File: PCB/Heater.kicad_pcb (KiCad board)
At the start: 2 copper layers, 29 parts, among them IC1 ATTINY45-P, P1 220V 50Hz, P2 ICP, P3 DS18B20, T1 SCR

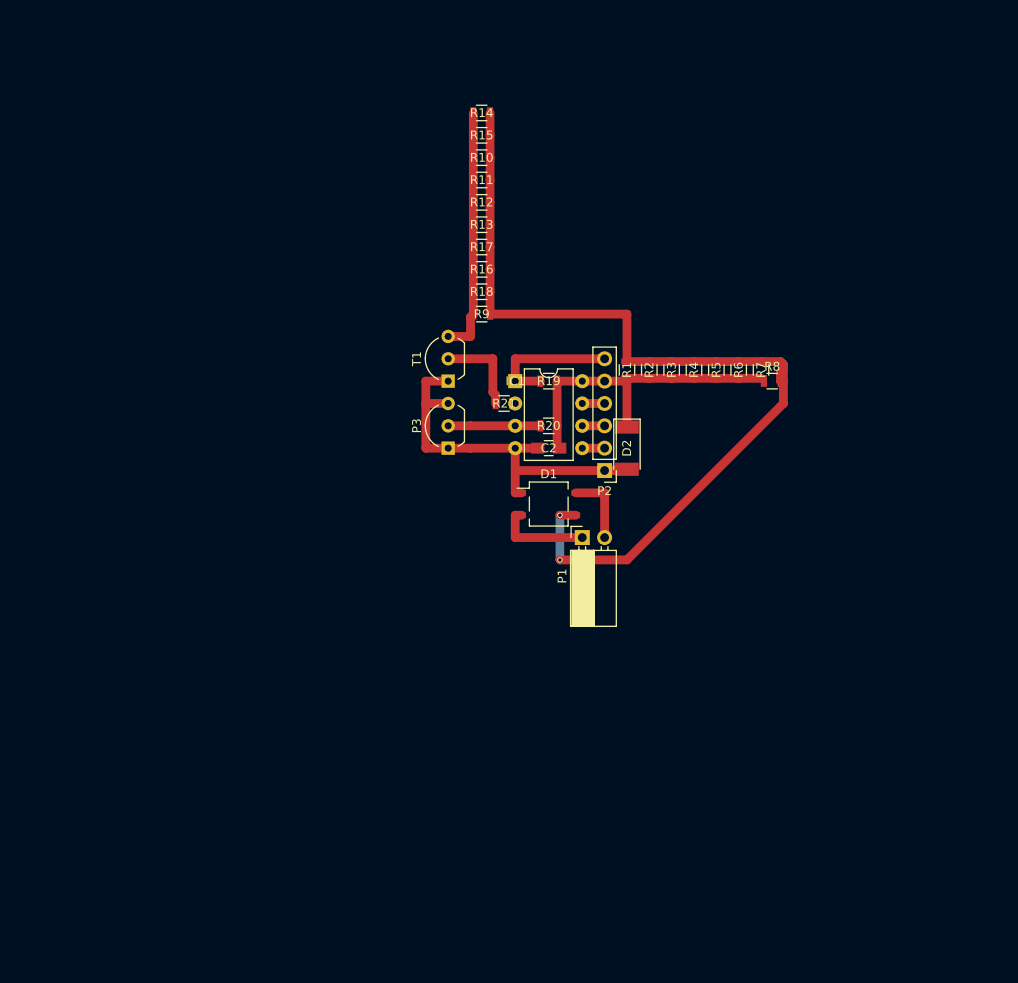
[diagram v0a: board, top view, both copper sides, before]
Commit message: Updated Schematic and PCB to use optotriac
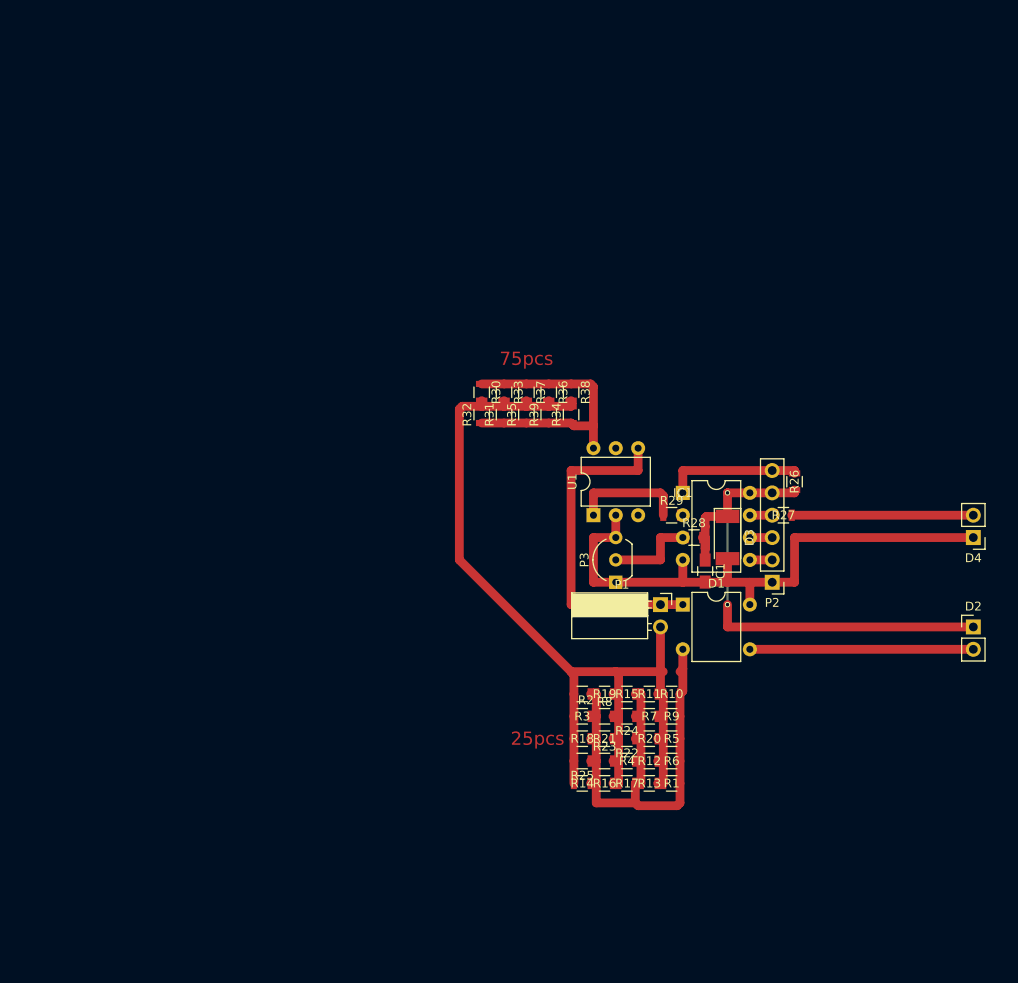
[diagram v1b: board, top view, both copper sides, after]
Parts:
- removed C2: 10u, Capacitors_SMD:C_0805_HandSoldering
- removed T1: SCR, TO_SOT_Packages_THT:TO-92_Inline_Wide
- added C1: 10u, Capacitors_SMD:C_0805_HandSoldering, F.Cu at (114.3, 94.0)
- added D3: ZD5V, Diodes_SMD:D_MELF, F.Cu at (116.8, 90.2)
- added D4: LED, Socket_Strips:Socket_Strip_Straight_1x02_Pitch2.54mm, F.Cu at (144.8, 90.2)
- added R22: 560K, Resistors_SMD:R_0805, F.Cu at (105.4, 113.0)
- added R23: 560K, Resistors_SMD:R_0805, F.Cu at (102.9, 115.6)
- added R24: 560K, Resistors_SMD:R_0805, F.Cu at (105.4, 110.5)
- added R25: 560K, Resistors_SMD:R_0805, F.Cu at (100.3, 115.6)
- added R26: 10K, Resistors_SMD:R_0805, F.Cu at (124.5, 83.8)
- added R27: 2K2, Resistors_SMD:R_0805, F.Cu at (123.2, 87.6)
- added R28: 5K, Resistors_SMD:R_0805, F.Cu at (113.0, 90.2)
- added R29: 470R, Resistors_SMD:R_0805, F.Cu at (110.5, 87.6)
- added R30: 560K, Resistors_SMD:R_0805, F.Cu at (88.9, 73.7)
- added R31: 560K, Resistors_SMD:R_0805, F.Cu at (91.4, 76.2)
- added R32: 560K, Resistors_SMD:R_0805, F.Cu at (88.9, 76.2)
- added R33: 560K, Resistors_SMD:R_0805, F.Cu at (91.4, 73.7)
- added R34: 560K, Resistors_SMD:R_0805, F.Cu at (99.1, 76.2)
- added R35: 560K, Resistors_SMD:R_0805, F.Cu at (94.0, 76.2)
- added R36: 560K, Resistors_SMD:R_0805, F.Cu at (96.5, 73.7)
- added R37: 560K, Resistors_SMD:R_0805, F.Cu at (94.0, 73.7)
- added R38: 560K, Resistors_SMD:R_0805, F.Cu at (99.1, 73.7)
- added R39: 560K, Resistors_SMD:R_0805, F.Cu at (96.5, 76.2)
- added U1: MOC3023M, Housings_DIP:DIP-6_W7.62mm, F.Cu at (101.6, 87.6)
- D1: value Diode_Bridge -> Graetz; footprint Diodes_SMD:Diode_Bridge_TO-269AA -> diodebridge:DIP-6_W7.62mm
- D2: value ZD5V -> LED; footprint Diodes_SMD:D_MELF -> Socket_Strips:Socket_Strip_Straight_1x02_Pitch2.54mm
- R19, R21: value 10K -> 560K
- R20: value 5K -> 560K
- moved R14 77.1 mm to (100.3, 118.1)
- moved R12 66.3 mm to (108.0, 115.6), turned to 0 degrees
- moved R13 66.3 mm to (108.0, 118.1), turned to 0 degrees
- moved R15 65.6 mm to (105.4, 108.0)
- moved R10 64.7 mm to (110.5, 108.0)
- moved R17 63.2 mm to (105.4, 118.1)
- moved R11 61.4 mm to (108.0, 108.0), turned to 0 degrees
- moved R16 60.1 mm to (102.9, 118.1), turned to 0 degrees
- moved R18 52.1 mm to (100.3, 113.0)
- moved R9 50.6 mm to (110.5, 110.5)
- moved R1 47.3 mm to (110.5, 118.1), turned to 180 degrees
- moved R4 45.1 mm to (105.4, 115.6), turned to 180 degrees
- moved R6 45.1 mm to (110.5, 115.6), turned to 180 degrees
- moved D2 44.3 mm to (144.8, 100.3), turned to 0 degrees
- moved R8 42.6 mm to (102.9, 110.5)
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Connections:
- D1 pad 1: GNDREF -> Net-(D1-Pad1)
- D1 pad 4: Net-(D1-Pad4) -> GNDREF
- D2 pad 1: Net-(C2-Pad1) -> Net-(C1-Pad1)
- D2 pad 2: GNDREF -> Net-(D1-Pad3)
- IC1 pad 8: Net-(C2-Pad1) -> Net-(C1-Pad1)
- P1 pad 1: Net-(D1-Pad2) -> Net-(D1-Pad1)
- P1 pad 2: Net-(D1-Pad4) -> Net-(P1-Pad2)
- P2 pad 5: Net-(C2-Pad1) -> Net-(C1-Pad1)
- R1 pad 1: Net-(C2-Pad1) -> Net-(D1-Pad2)
- R1 pad 2: Net-(D1-Pad3) -> Net-(P1-Pad2)
- R10 pad 1: Net-(D1-Pad3) -> Net-(D1-Pad2)
- R10 pad 2: Net-(R10-Pad2) -> Net-(P1-Pad2)
- R11 pad 1: Net-(D1-Pad3) -> Net-(D1-Pad2)
- R11 pad 2: Net-(R10-Pad2) -> Net-(P1-Pad2)
- R12 pad 1: Net-(D1-Pad3) -> Net-(D1-Pad2)
- R12 pad 2: Net-(R10-Pad2) -> Net-(P1-Pad2)
- R13 pad 1: Net-(D1-Pad3) -> Net-(D1-Pad2)
- R13 pad 2: Net-(R10-Pad2) -> Net-(P1-Pad2)
- R14 pad 1: Net-(D1-Pad3) -> Net-(D1-Pad2)
- R14 pad 2: Net-(R10-Pad2) -> Net-(P1-Pad2)
- R15 pad 1: Net-(D1-Pad3) -> Net-(D1-Pad2)
- R15 pad 2: Net-(R10-Pad2) -> Net-(P1-Pad2)
- R16 pad 1: Net-(D1-Pad3) -> Net-(D1-Pad2)
- R16 pad 2: Net-(R10-Pad2) -> Net-(P1-Pad2)
- R17 pad 1: Net-(D1-Pad3) -> Net-(D1-Pad2)
- R17 pad 2: Net-(R10-Pad2) -> Net-(P1-Pad2)
- R18 pad 1: Net-(D1-Pad3) -> Net-(D1-Pad2)
- R18 pad 2: Net-(R10-Pad2) -> Net-(P1-Pad2)
- R19 pad 1: Net-(IC1-Pad1) -> Net-(D1-Pad2)
- R19 pad 2: Net-(C2-Pad1) -> Net-(P1-Pad2)
- R2 pad 1: Net-(C2-Pad1) -> Net-(D1-Pad2)
- R2 pad 2: Net-(D1-Pad3) -> Net-(P1-Pad2)
- R20 pad 1: Net-(IC1-Pad3) -> Net-(D1-Pad2)
- R20 pad 2: Net-(C2-Pad1) -> Net-(P1-Pad2)
- R21 pad 1: Net-(R21-Pad1) -> Net-(D1-Pad2)
- R21 pad 2: Net-(IC1-Pad2) -> Net-(P1-Pad2)
- R3 pad 1: Net-(C2-Pad1) -> Net-(D1-Pad2)
- R3 pad 2: Net-(D1-Pad3) -> Net-(P1-Pad2)
- R4 pad 1: Net-(C2-Pad1) -> Net-(D1-Pad2)
- R4 pad 2: Net-(D1-Pad3) -> Net-(P1-Pad2)
- R5 pad 1: Net-(C2-Pad1) -> Net-(D1-Pad2)
- R5 pad 2: Net-(D1-Pad3) -> Net-(P1-Pad2)
- R6 pad 1: Net-(C2-Pad1) -> Net-(D1-Pad2)
- R6 pad 2: Net-(D1-Pad3) -> Net-(P1-Pad2)
- R7 pad 1: Net-(C2-Pad1) -> Net-(D1-Pad2)
- R7 pad 2: Net-(D1-Pad3) -> Net-(P1-Pad2)
- R8 pad 1: Net-(C2-Pad1) -> Net-(D1-Pad2)
- R8 pad 2: Net-(D1-Pad3) -> Net-(P1-Pad2)
- R9 pad 1: Net-(D1-Pad3) -> Net-(D1-Pad2)
- R9 pad 2: Net-(R10-Pad2) -> Net-(P1-Pad2)
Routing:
- net Net-(P1-Pad2): track 0.00 -> 112.0 mm
- net Net-(D1-Pad3): track 107.5 -> 25.4 mm, vias 2 -> 0
- net Net-(C1-Pad1): track 0.00 -> 62.8 mm, vias 0 -> 2
- net Net-(D1-Pad2): track 10.9 -> 59.0 mm
- net Net-(D1-Pad1): track 0.00 -> 38.1 mm
- net Net-(C2-Pad1): track 36.1 -> 0.00 mm
- net Net-(R30-Pad1): track 0.00 -> 32.6 mm
- net Net-(R10-Pad2): track 28.1 -> 0.00 mm
- net GNDREF: track 44.0 -> 66.2 mm
- net Net-(D4-Pad2): track 0.00 -> 20.6 mm
- net Net-(R29-Pad1): track 0.00 -> 12.8 mm
- net Net-(R21-Pad1): track 10.3 -> 0.00 mm
- net Net-(D1-Pad4): track 8.36 -> 0.00 mm
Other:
- board text added: "25pcs"
- board text added: "75pcs"

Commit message: Added fw
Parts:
- D1: footprint diodebridge:DIP-6_W7.62mm -> Diodes_SMD:Diode_Bridge_TO-269AA
- D3: footprint Diodes_SMD:D_MELF -> Diodes_SMD:D_MELF_Handsoldering
- moved D3 9.92 mm to (124.5, 96.5), turned to 90 degrees
- moved C1 9.16 mm to (121.9, 99.1), turned to 90 degrees
- moved D1 4.02 mm to (115.6, 99.1)
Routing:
- net Net-(C1-Pad1): track 62.8 -> 82.7 mm, vias 2 -> 0
- net GNDREF: track 66.2 -> 69.7 mm
- net Net-(D1-Pad3): track 25.4 -> 28.2 mm
- net Net-(D1-Pad2): track 59.0 -> 61.8 mm
- net Net-(D1-Pad1): track 38.1 -> 38.8 mm

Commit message: Not working yet
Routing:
- net Net-(P1-Pad2): track 112.0 -> 152.1 mm
- net Net-(D1-Pad2): track 61.8 -> 61.1 mm
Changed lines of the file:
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@@
-(kicad_pcb (version 4) (host pcbnew 4.0.4+e1-6308~48~ubuntu16.04.1-stable)
+(kicad_pcb (version 4) (host pcbnew 4.0.6-e0-6349~53~ubuntu16.04.1)
   (general
     (links 98)
     (no_connects 0)
-    (area 0 0 0 0)
+    (area 85.659999 68.65 148.020002 121.350002)
     (thickness 1.6)
     (drawings 2)
-    (tracks 156)
+    (tracks 157)
     (zones 0)
     (modules 49)
@@
     (effects (font (size 1.5 1.5) (thickness 0.3)))
   )
-  (segment (start 119.38 97.79) (end 118.645 97.79) (width 0.25) (layer F.Cu) (net 1) (status 800000))
+  (segment (start 119.38 97.79) (end 118.645 97.79) (width 0.25) (layer F.Cu) (net 1))
   (segment (start 124.46 93.12) (end 124.46 90.17) (width 1) (layer F.Cu) (net 1))
   (segment (start 119.38 97.79) (end 121.9 97.79) (width 1) (layer F.Cu) (net 1))
@@
   (segment (start 116.84 95.25) (end 119.38 95.25) (width 1) (layer F.Cu) (net 1))
   (segment (start 119.38 95.25) (end 121.92 95.25) (width 1) (layer F.Cu) (net 1))
+  (segment (start 106.68 105.41) (end 101.6 105.41) (width 1) (layer F.Cu) (net 2))
+  (segment (start 101.92 105.73) (end 101.92 107.95) (width 1) (layer F.Cu) (net 2) (status 800000))
+  (segment (start 101.6 105.41) (end 101.92 105.73) (width 1) (layer F.Cu) (net 2))
+  (segment (start 111.76 105.41) (end 106.68 105.41) (width 1) (layer F.Cu) (net 2))
+  (segment (start 107 105.73) (end 107 107.95) (width 1) (layer F.Cu) (net 2) (status 800000))
+  (segment (start 106.68 105.41) (end 107 105.73) (width 1) (layer F.Cu) (net 2))
   (segment (start 111.76 102.87) (end 111.76 101.065) (width 1) (layer F.Cu) (net 2))
-  (segment (start 111.76 105.09) (end 111.76 102.87) (width 1) (layer F.Cu) (net 2))
-  (segment (start 111.76 101.065) (end 112.495 100.33) (width 1) (layer F.Cu) (net 2) (status 800000))
+  (segment (start 111.76 105.09) (end 111.76 105.41) (width 1) (layer F.Cu) (net 2))
+  (segment (start 111.76 105.41) (end 111.76 102.87) (width 1) (layer F.Cu) (net 2))
+  (segment (start 111.76 101.065) (end 112.495 100.33) (width 1) (layer F.Cu) (net 2))
   (segment (start 101.92 118.11) (end 101.28 118.11) (width 1) (layer F.Cu) (net 2))
   (segment (start 101.92 115.57) (end 101.28 115.57) (width 1) (layer F.Cu) (net 2))
@@
   (segment (start 101.92 110.49) (end 101.28 110.49) (width 1) (layer F.Cu) (net 2))
   (segment (start 101.92 107.95) (end 101.28 107.95) (width 1) (layer F.Cu) (net 2))
-  (segment (start 106.36 120.33) (end 101.92 120.33) (width 1) (layer F.Cu) (net 2))
-  (segment (start 101.92 120.33) (end 101.92 118.11) (width 1) (layer F.Cu) (net 2))
-  (segment (start 111.44 118.11) (end 111.44 120.33) (width 1) (layer F.Cu) (net 2))
-  (segment (start 106.36 120.33) (end 106.36 118.11) (width 1) (layer F.Cu) (net 2))
-  (segment (start 106.68 120.65) (end 106.36 120.33) (width 1) (layer F.Cu) (net 2))
-  (segment (start 111.12 120.65) (end 106.68 120.65) (width 1) (layer F.Cu) (net 2))
-  (segment (start 111.44 120.33) (end 111.12 120.65) (width 1) (layer F.Cu) (net 2))
   (segment (start 101.92 110.49) (end 101.92 107.95) (width 1) (layer F.Cu) (net 2))
   (segment (start 101.92 113.03) (end 101.92 110.49) (width 1) (layer F.Cu) (net 2))
@@
   (segment (start 111.76 105.09) (end 111.76 107.63) (width 1) (layer F.Cu) (net 2))
   (segment (start 111.76 107.63) (end 111.44 107.95) (width 1) (layer F.Cu) (net 2))
-  (segment (start 111.76 105.09) (end 111.44 105.41) (width 1) (layer F.Cu) (net 2))
-  (segment (start 118.645 100.33) (end 118.645 102.135) (width 1) (layer F.Cu) (net 3) (status 400000))
+  (segment (start 118.645 100.33) (end 118.645 102.135) (width 1) (layer F.Cu) (net 3))
   (segment (start 119.38 102.87) (end 144.78 102.87) (width 1) (layer F.Cu) (net 3))
   (segment (start 118.645 102.135) (end 119.38 102.87) (width 1) (layer F.Cu) (net 3))
@@
   (segment (start 119.38 85.09) (end 121.92 85.09) (width 1) (layer F.Cu) (net 10))
   (segment (start 124.14 87.63) (end 144.78 87.63) (width 1) (layer F.Cu) (net 11))
+  (segment (start 86.36 97.79) (end 86.36 118.11) (width 1) (layer F.Cu) (net 12))
+  (segment (start 88.58 120.33) (end 99.38 120.33) (width 1) (layer F.Cu) (net 12))
+  (segment (start 86.36 118.11) (end 88.58 120.33) (width 1) (layer F.Cu) (net 12))
+  (segment (start 109.22 100.33) (end 88.9 100.33) (width 1) (layer F.Cu) (net 12) (status 400000))
+  (segment (start 86.68 75.25) (end 88.9 75.25) (width 1) (layer F.Cu) (net 12) (status 800000))
+  (segment (start 86.36 74.93) (end 86.68 75.25) (width 1) (layer F.Cu) (net 12))
+  (segment (start 86.36 97.79) (end 86.36 74.93) (width 1) (layer F.Cu) (net 12))
+  (segment (start 88.9 100.33) (end 86.36 97.79) (width 1) (layer F.Cu) (net 12))
+  (segment (start 104.46 120.33) (end 99.38 120.33) (width 1) (layer F.Cu) (net 12))
+  (segment (start 99.38 120.33) (end 99.38 118.11) (width 1) (layer F.Cu) (net 12) (status 800000))
+  (segment (start 109.54 118.11) (end 109.54 120.33) (width 1) (layer F.Cu) (net 12) (status 400000))
+  (segment (start 104.46 120.33) (end 104.46 118.11) (width 1) (layer F.Cu) (net 12) (status 800000))
+  (segment (start 104.14 120.65) (end 104.46 120.33) (width 1) (layer F.Cu) (net 12))
+  (segment (start 109.22 120.65) (end 104.14 120.65) (width 1) (layer F.Cu) (net 12))
+  (segment (start 109.54 120.33) (end 109.22 120.65) (width 1) (layer F.Cu) (net 12))
   (segment (start 88.9 75.25) (end 88.9 74.61) (width 1) (layer F.Cu) (net 12))
   (segment (start 91.44 75.25) (end 91.44 74.61) (width 1) (layer F.Cu) (net 12))
@@
   (segment (start 96.52 75.25) (end 96.52 74.61) (width 1) (layer F.Cu) (net 12))
   (segment (start 99.06 75.25) (end 99.06 74.61) (width 1) (layer F.Cu) (net 12))
-  (segment (start 88.9 75.25) (end 86.68 75.25) (width 1) (layer F.Cu) (net 12))
-  (segment (start 86.36 92.71) (end 99.38 105.73) (width 1) (layer F.Cu) (net 12))
-  (segment (start 86.36 75.57) (end 86.36 92.71) (width 1) (layer F.Cu) (net 12))
-  (segment (start 86.68 75.25) (end 86.36 75.57) (width 1) (layer F.Cu) (net 12))
-  (segment (start 104.14 105.41) (end 99.06 105.41) (width 1) (layer F.Cu) (net 12))
-  (segment (start 99.06 105.41) (end 99.38 105.73) (width 1) (layer F.Cu) (net 12))
-  (segment (start 99.38 105.73) (end 99.38 107.95) (width 1) (layer F.Cu) (net 12))
-  (segment (start 109.22 105.41) (end 104.14 105.41) (width 1) (layer F.Cu) (net 12))
-  (segment (start 104.46 105.73) (end 104.46 107.95) (width 1) (layer F.Cu) (net 12))
-  (segment (start 104.14 105.41) (end 104.46 105.73) (width 1) (layer F.Cu) (net 12))
   (segment (start 99.38 115.57) (end 99.38 118.11) (width 1) (layer F.Cu) (net 12))
   (segment (start 99.38 113.03) (end 99.38 115.57) (width 1) (layer F.Cu) (net 12))
@@
   (segment (start 104.46 115.57) (end 104.46 113.03) (width 1) (layer F.Cu) (net 12))
   (segment (start 104.46 118.11) (end 104.46 115.57) (width 1) (layer F.Cu) (net 12))
-  (segment (start 109.22 105.41) (end 109.22 107.63) (width 1) (layer F.Cu) (net 12))
   (segment (start 109.22 107.63) (end 109.54 107.95) (width 1) (layer F.Cu) (net 12))
-  (segment (start 109.22 105.41) (end 109.54 105.41) (width 1) (layer F.Cu) (net 12))
   (segment (start 109.54 110.49) (end 109.54 107.95) (width 1) (layer F.Cu) (net 12))
   (segment (start 109.54 113.03) (end 109.54 110.49) (width 1) (layer F.Cu) (net 12))
   (segment (start 109.54 115.57) (end 109.54 113.03) (width 1) (layer F.Cu) (net 12))
   (segment (start 109.54 118.11) (end 109.54 115.57) (width 1) (layer F.Cu) (net 12))
-  (segment (start 109.22 100.33) (end 109.22 105.41) (width 1) (layer F.Cu) (net 12))
   (segment (start 109.54 87.63) (end 109.54 85.41) (width 1) (layer F.Cu) (net 13))
   (segment (start 101.6 85.09) (end 101.6 87.63) (width 1) (layer F.Cu) (net 13))
@@
   (segment (start 101.6 77.47) (end 99.38 77.47) (width 1) (layer F.Cu) (net 14))
   (segment (start 99.38 77.47) (end 99.06 77.15) (width 1) (layer F.Cu) (net 14))
-  (segment (start 112.495 97.79) (end 111.76 97.79) (width 1) (layer F.Cu) (net 15) (status 400000))
+  (segment (start 112.495 97.79) (end 111.76 97.79) (width 1) (layer F.Cu) (net 15))
   (segment (start 111.76 97.79) (end 109.22 97.79) (width 1) (layer F.Cu) (net 15))
   (segment (start 106.68 80.01) (end 106.68 82.55) (width 1) (layer F.Cu) (net 15))

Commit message: finished working version of the PCB and FW
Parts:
- added J1: GND, Pin_Headers:Pin_Header_Straight_1x01_Pitch1.27mm, F.Cu at (111.8, 95.2)
- added J2: RST, Pin_Headers:Pin_Header_Straight_1x01_Pitch1.27mm, F.Cu at (111.8, 82.5)
- P2: value ICP -> CONN_01X04; footprint Socket_Strips:Socket_Strip_Straight_1x06_Pitch2.54mm -> Pin_Headers:Pin_Header_Straight_1x04_Pitch2.54mm
- moved D2 22.9 mm to (121.9, 101.6), turned to 270 degrees
- moved D4 20.3 mm to (124.5, 90.2)
- moved P1 16.1 mm to (94.0, 92.7)
- moved R26 14.0 mm to (110.5, 85.1), turned to 180 degrees
- moved P3 13.0 mm to (101.6, 82.5), turned to 0 degrees
- moved R30 9.38 mm to (93.3, 81.9), turned to 0 degrees
- moved R32 9.03 mm to (95.9, 81.9), turned to 180 degrees
- moved U1 7.18 mm to (106.7, 92.7), turned to 180 degrees
- moved R33 6.02 mm to (93.3, 79.4), turned to 0 degrees
- moved R38 6.02 mm to (93.3, 71.8), turned to 0 degrees
- moved R31 5.46 mm to (95.9, 79.4), turned to 180 degrees
- moved R34 5.46 mm to (95.9, 71.8), turned to 180 degrees
- moved R28 5.39 mm to (109.2, 86.4), turned to 90 degrees
- moved R36 3.24 mm to (93.3, 74.3), turned to 0 degrees
- moved R37 3.24 mm to (93.3, 76.8), turned to 0 degrees
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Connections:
- P2 pad 1: GNDREF -> Net-(IC1-Pad5)
- P2 pad 2: Net-(IC1-Pad5) -> Net-(IC1-Pad6)
- P2 pad 3: Net-(IC1-Pad6) -> Net-(IC1-Pad7)
- P2 pad 4: Net-(IC1-Pad7) -> Net-(C1-Pad1)
- P3 pad 2: Net-(IC1-Pad3) -> Net-(IC1-Pad2)
- R28 pad 1: Net-(IC1-Pad3) -> Net-(IC1-Pad2)
- R29 pad 2: Net-(IC1-Pad2) -> Net-(IC1-Pad3)
- U1 pad 4: Net-(D1-Pad1) -> Net-(R30-Pad1)
- U1 pad 6: Net-(R30-Pad1) -> Net-(D1-Pad1)
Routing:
- net Net-(P1-Pad2): track 152.1 -> 108.4 mm
- net Net-(D1-Pad3): track 28.2 -> 1.57 mm
- net Net-(C1-Pad1): track 82.7 -> 57.2 mm
- net Net-(D4-Pad2): track 20.6 -> 0.00 mm
- net Net-(D1-Pad1): track 38.8 -> 23.6 mm
- net Net-(IC1-Pad2): track 0.00 -> 13.3 mm
- net Net-(IC1-Pad1): track 15.6 -> 2.54 mm
- net Net-(IC1-Pad3): track 10.2 -> 0.00 mm
- net Net-(R29-Pad1): track 12.8 -> 5.21 mm
- net Net-(R30-Pad1): track 32.6 -> 37.7 mm
- net GNDREF: track 69.7 -> 67.2 mm
